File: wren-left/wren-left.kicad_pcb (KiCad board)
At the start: 2 copper layers, 230.3 x 117 mm, 93 parts, among them J1 TRRS_Jack, SW0 Reset, U1 ProMicro

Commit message: Tracks Finished
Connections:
- U1 pad 1: COL9 -> ROW0
- U1 pad 10: ROW3 -> COL9
- U1 pad 11: ROW4 -> Net-(U1-Pad11)
- U1 pad 12: Net-(U1-Pad12) -> ROW4
- U1 pad 2: COL8 -> ROW1
- U1 pad 7: ROW0 -> ROW2
- U1 pad 8: ROW1 -> ROW3
- U1 pad 9: ROW2 -> COL8
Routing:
- net GND: track 8.26 -> 85.2 mm, vias 2 -> 4
- net COL7: track 151.1 -> 210.2 mm, vias 1 -> 2
- net ROW1: track 186.9 -> 222.3 mm, vias 0 -> 1
- net ROW2: track 216.8 -> 227.9 mm, vias 0 -> 1
- net SDA: track 85.4 -> 78.1 mm, vias 1 -> 0
- net ROW3: track 238.4 -> 244.9 mm, vias 0 -> 1
- net COL2: track 143.5 -> 149.9 mm, vias 1 -> 3
- net SCL: track 61.1 -> 67.0 mm, vias 1 -> 4
- net COL3: track 160.3 -> 164.6 mm, vias 1 -> 0
- net ROW4: track 134.6 -> 131.7 mm, vias 0 -> 1
- net COL8: track 245.9 -> 247.9 mm, vias 0 -> 1
- net ROW0: track 209.8 -> 211.7 mm, vias 0 -> 1
- net VCC: track 73.7 -> 75.4 mm
- net COL0: track 108.2 -> 109.9 mm, vias 0 -> 1
- net COL1: track 124.1 -> 125.5 mm
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
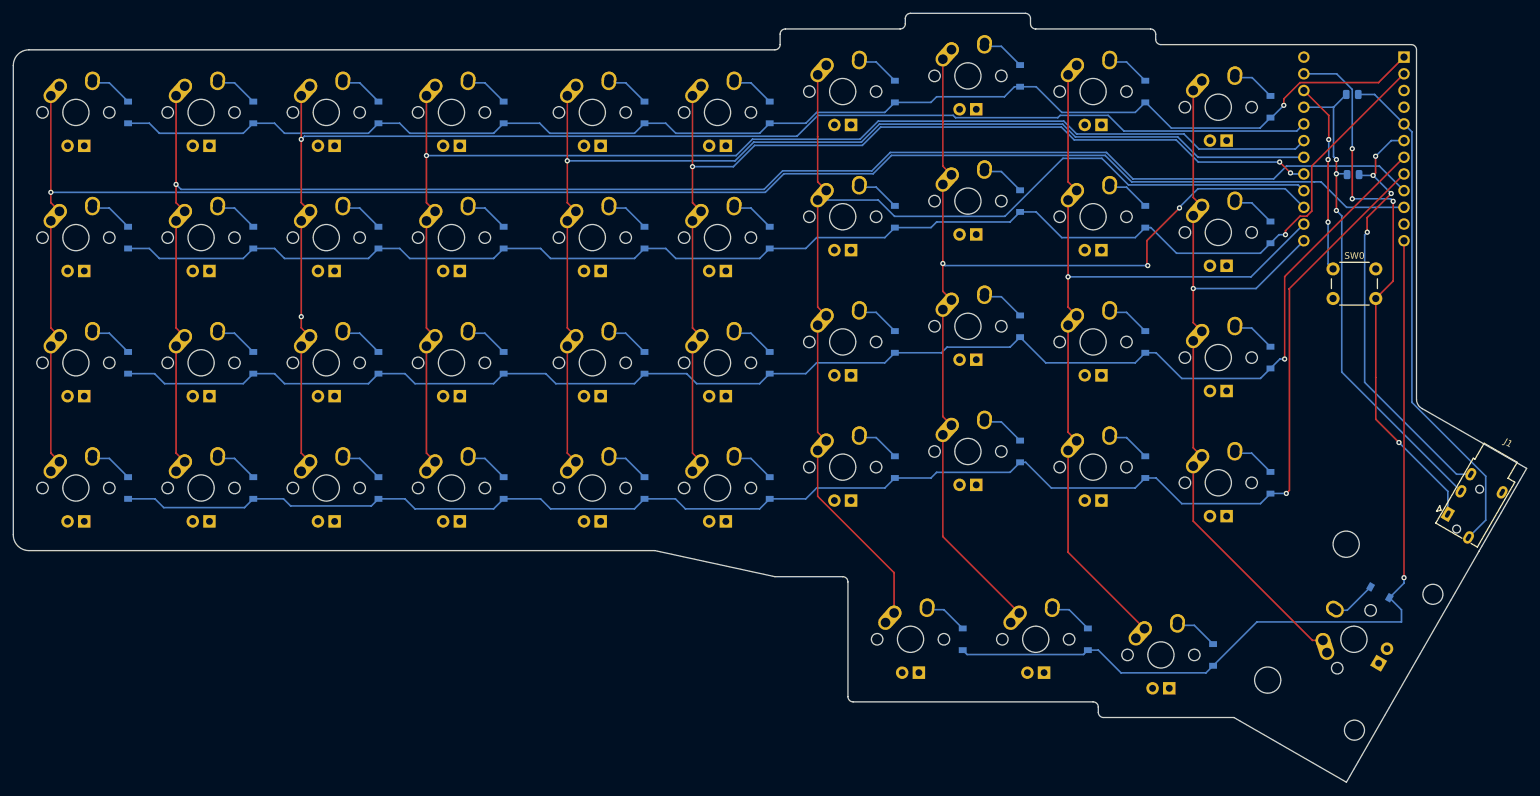
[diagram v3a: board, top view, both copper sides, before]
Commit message: Add PCB Mount Holes
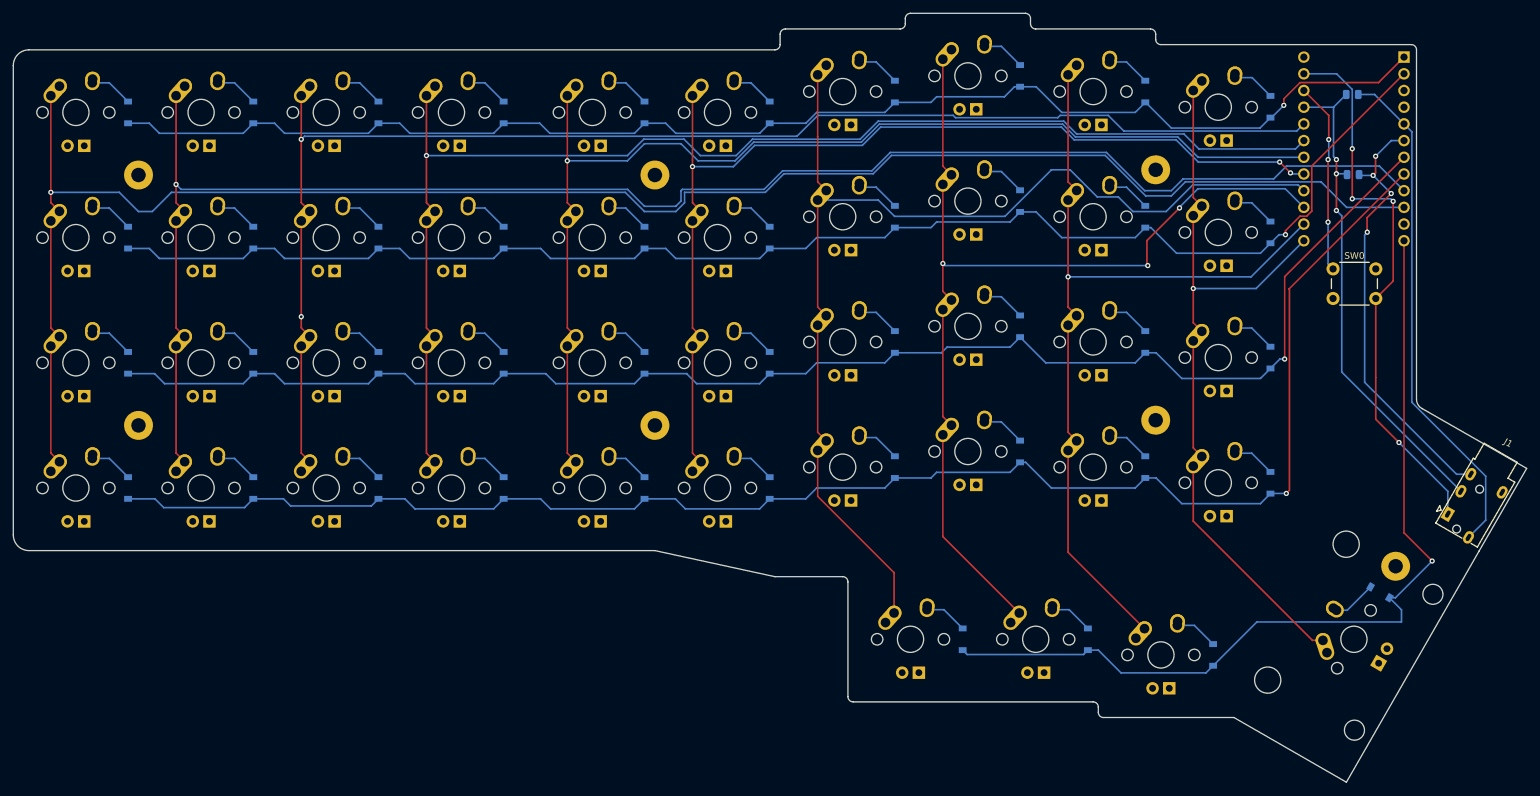
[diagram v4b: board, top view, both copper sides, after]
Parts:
- added REF**: MountingHole_2.2mm_M2_Pad, MountingHole:MountingHole_2.2mm_M2_Pad, F.Cu at (56.4, 46.0)
- added REF**: MountingHole_2.2mm_M2_Pad, MountingHole:MountingHole_2.2mm_M2_Pad, F.Cu at (56.4, 84.1)
- added REF**: MountingHole_2.2mm_M2_Pad, MountingHole:MountingHole_2.2mm_M2_Pad, F.Cu at (134.9, 84.1)
- added REF**: MountingHole_2.2mm_M2_Pad, MountingHole:MountingHole_2.2mm_M2_Pad, F.Cu at (134.9, 46.0)
- added REF**: MountingHole_2.2mm_M2_Pad, MountingHole:MountingHole_2.2mm_M2_Pad, F.Cu at (211.1, 45.2)
- added REF**: MountingHole_2.2mm_M2_Pad, MountingHole:MountingHole_2.2mm_M2_Pad, F.Cu at (211.1, 83.3)
- added REF**: MountingHole_2.2mm_M2_Pad, MountingHole:MountingHole_2.2mm_M2_Pad, F.Cu at (247.7, 105.6)
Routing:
- net COL9: track 265.9 -> 273.4 mm
- net COL8: track 247.9 -> 252.5 mm
- net ROW4: track 131.7 -> 135.7 mm
- net COL5: track 170.9 -> 173.0 mm
- net COL6: track 192.4 -> 194.4 mm
- net COL3: track 164.6 -> 166.6 mm

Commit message: Switch to Elite C Footprints
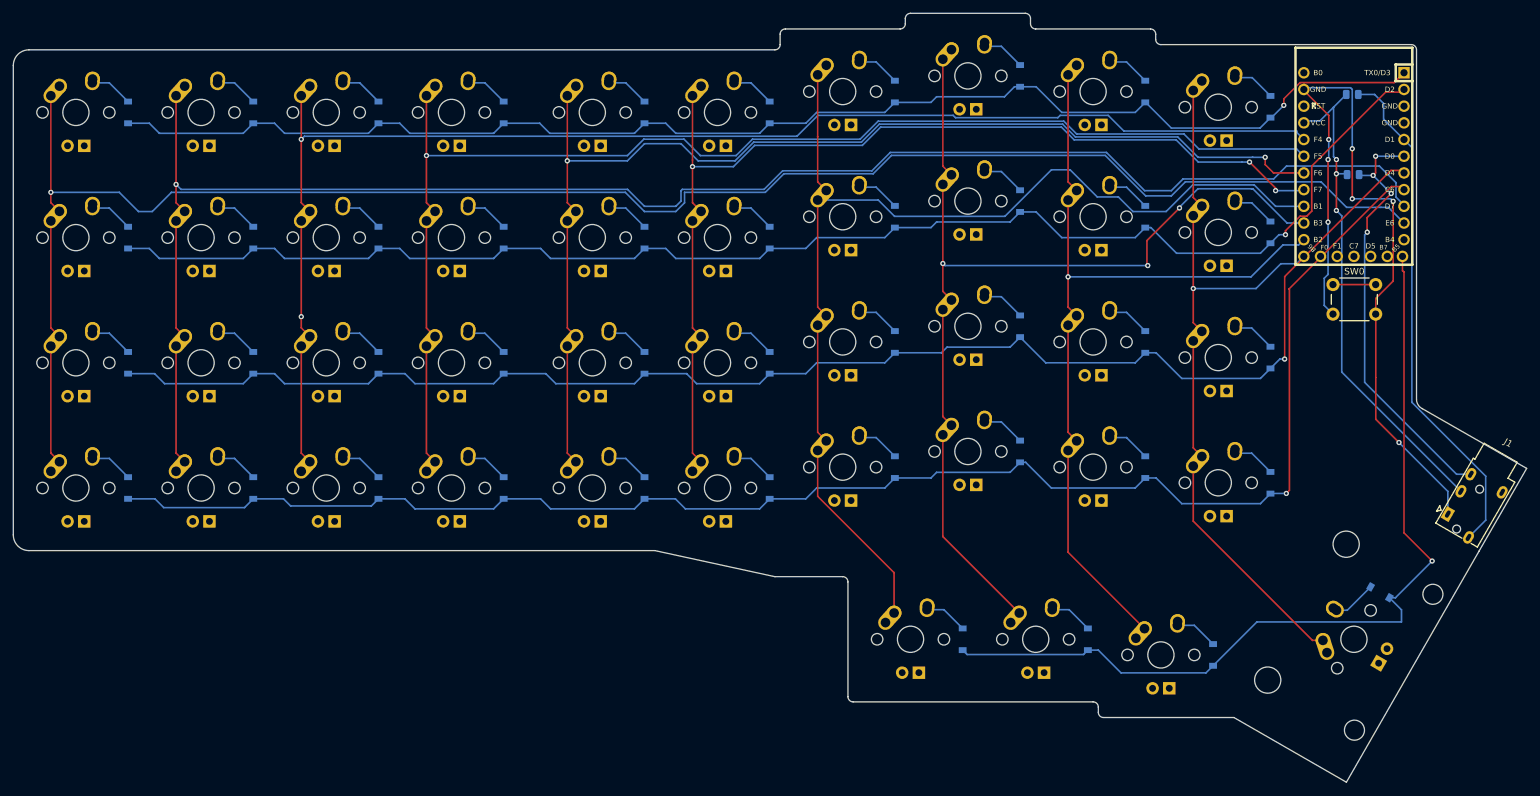
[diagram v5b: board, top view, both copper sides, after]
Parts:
- removed REF** (x7): MountingHole_2.2mm_M2_Pad, MountingHole:MountingHole_2.2mm_M2_Pad
- U1: value ProMicro -> Elite-C; footprint footprints:ARDUINO_PRO_MICRO -> footprints:Elite-C
- moved SW0 2.38 mm to (238.1, 62.7)
- moved U1 2.38 mm to (241.3, 44.5)
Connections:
- U1 pad 11: Net-(U1-Pad11) -> (no net)
- U1 pad 24: Net-(U1-Pad24) -> (no net)
- U1 pad 3: Net-(U1-Pad3) -> (no net)
- U1 pad 4: Net-(U1-Pad4) -> (no net)
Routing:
- net GND: track 85.2 -> 120.7 mm, vias 4 -> 7
- net Net-(SW0-Pad1): track 30.0 -> 6.50 mm, vias 3 -> 0
- net ROW4: track 135.7 -> 133.5 mm
- net COL8: track 252.5 -> 254.6 mm
- net COL5: track 173.0 -> 174.7 mm, vias 1 -> 2
- net COL4: track 152.9 -> 154.2 mm
- net COL3: track 166.6 -> 167.5 mm
- net COL1: track 125.5 -> 124.5 mm
- net SCL: track 67.0 -> 66.0 mm
- net COL0: track 109.9 -> 108.9 mm
- net ROW1: track 222.3 -> 221.3 mm
- net ROW0: track 211.7 -> 210.7 mm
- net COL9: track 273.4 -> 274.4 mm
- net COL2: track 149.9 -> 150.9 mm
- net VCC: track 75.4 -> 76.3 mm
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
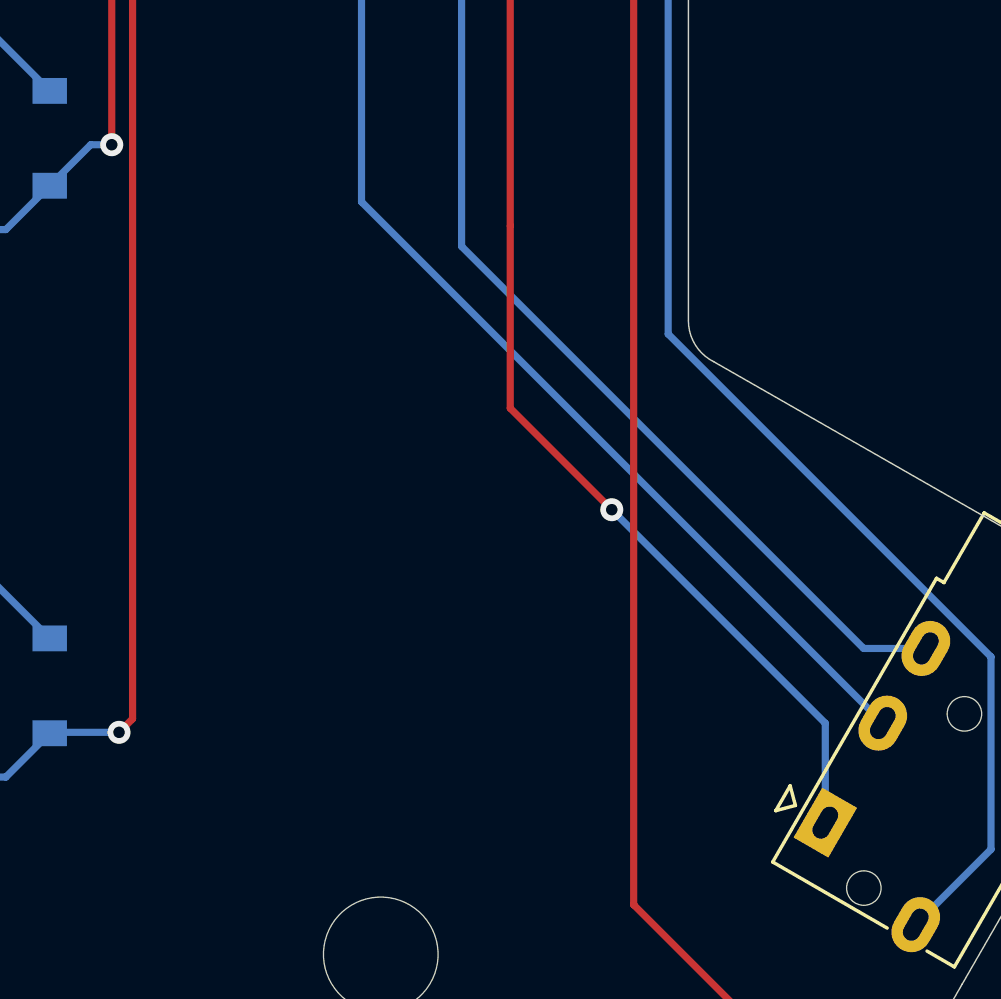
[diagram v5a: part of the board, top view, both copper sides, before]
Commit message: Add Encoders to PCB
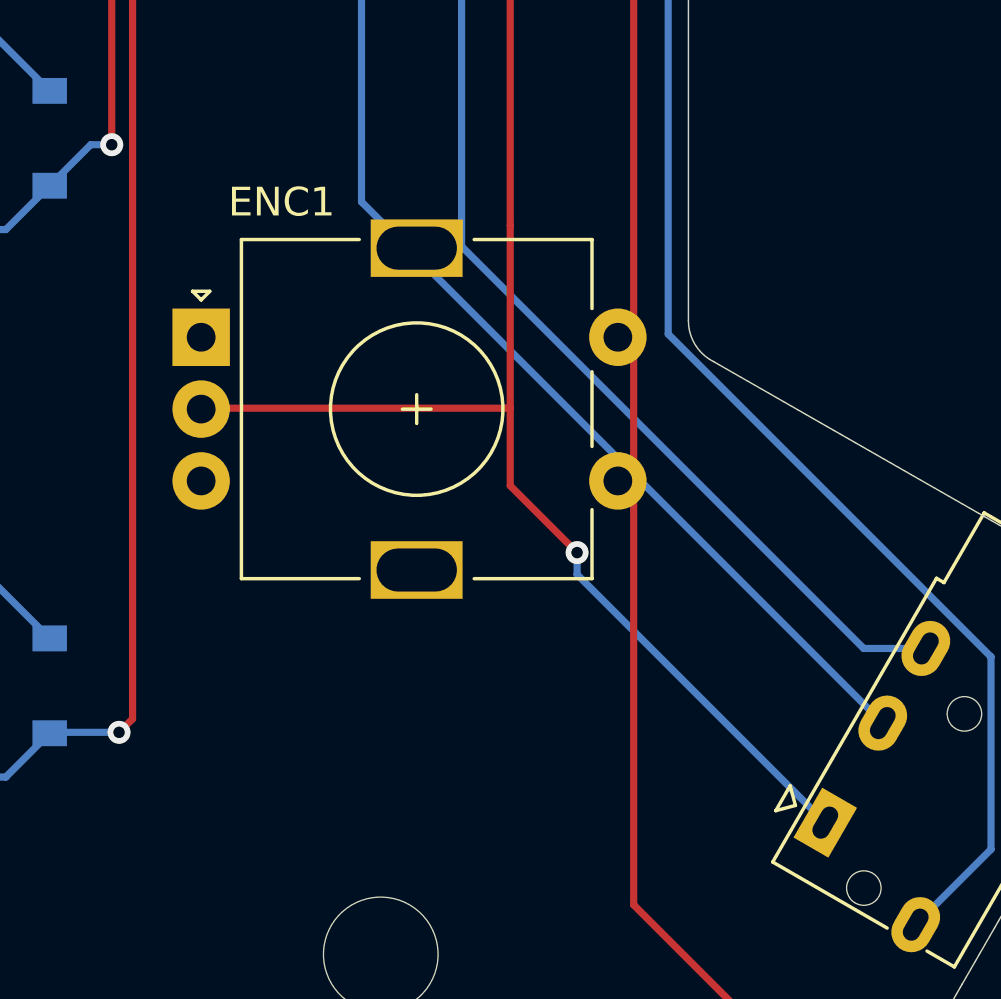
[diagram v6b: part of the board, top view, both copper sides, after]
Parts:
- added ENC1: Rotary_Encoder_Switch, Rotary_Encoder:RotaryEncoder_Alps_EC11E-Switch_Vertical_H20mm, F.Cu at (233.9, 80.7)
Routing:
- net GND: track 120.7 -> 131.5 mm

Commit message: Component Updates
Switch to through-hole diodes and resistors, reroute traces, etc.
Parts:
- added D41: D_Small, footprints:D_SOD123_axial, B.Cu at (248.3, 104.2)
- D1, D10, D11, D12, D13, D14, D15, D16, D17, D18, D19, D2, D20, D21, D22, D23, D24, D25, D26, D27, D28, D29, D3, D30, D31, D32, D33, D34, D35, D36, D37, D38, D39, D4, D40, D5, D6, D7, D8, D9: footprint Diode_SMD:D_SOD-123 -> footprints:D_SOD123_axial
- D42: renamed from D41; footprint Diode_SMD:D_SOD-123 -> footprints:D_SOD123_axial
- D43: renamed from D42; footprint Diode_SMD:D_SOD-123 -> footprints:D_SOD123_axial
- D44: renamed from D43; footprint Diode_SMD:D_SOD-123 -> footprints:D_SOD123_axial
- D45: renamed from D44; footprint Diode_SMD:D_SOD-123 -> footprints:D_SOD123_axial
- R1, R2: footprint Resistor_SMD:R_0805_2012Metric -> Resistor_THT:R_Axial_DIN0204_L3.6mm_D1.6mm_P1.90mm_Vertical
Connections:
- ENC1 pad S1: (no net) -> COL0
- ENC1 pad S2: (no net) -> ENC1-OUT
- MX41 pad 1: COL0 -> COL1
- MX42 pad 1: COL1 -> COL2
- MX43 pad 1: COL2 -> COL3
- MX44 pad 1: COL3 -> COL4
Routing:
- net ENC1-OUT: track 0.00 -> 22.9 mm
- net COL0: track 108.9 -> 107.3 mm
- net GND: track 131.5 -> 132.3 mm
- net ROW4: track 133.5 -> 132.9 mm, vias 1 -> 0

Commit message: Cleanup Work
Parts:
- R1, R2: footprint Resistor_THT:R_Axial_DIN0204_L3.6mm_D1.6mm_P1.90mm_Vertical -> Resistor_THT:R_Axial_DIN0204_L3.6mm_D1.6mm_P5.08mm_Vertical
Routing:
- net COL4: track 154.2 -> 199.5 mm, vias 3 -> 5
- net COL1: track 124.5 -> 148.7 mm, vias 1 -> 3
- net COL3: track 167.5 -> 183.9 mm, vias 0 -> 2
- net COL2: track 150.9 -> 166.3 mm, vias 3 -> 5
